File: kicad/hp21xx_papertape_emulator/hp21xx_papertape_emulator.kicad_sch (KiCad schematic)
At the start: 75 parts, among them J1 Micro_SD_Card_Det_Hirose_DM3AT, J2 HP Microcircuit, J3 SWD, J4 SERIAL, Q1 AO3401A, SW1 Up, SW2 Down, SW3 Select, U1 USBLC6-2SC6, U2 TLV75533PDRV, U3 74HCT245, U4 74LVC245, U5 74LVC1G04, U6 STM32F103C8Tx, U7 74AHC1GU04, Y1 8MHz

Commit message: Tried to create production files but it failed...
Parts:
- removed C5: 1u, Capacitor_SMD:C_0805_2012Metric, symbol Device:C_Small
- removed Q1: AO3401A, Package_TO_SOT_SMD:SOT-323_SC-70, symbol Simulation_SPICE:PMOS
- removed R18, R19: 4.7k, Resistor_SMD:R_0402_1005Metric, symbol Device:R_Small
- removed R23: 100k, Resistor_SMD:R_0402_1005Metric, symbol Device:R_Small
- removed R24: 10k, Resistor_SMD:R_0402_1005Metric, symbol Device:R_Small
- added C10, C8, C9: 100n, Capacitor_SMD:C_0402_1005Metric, symbol Device:C_Small
- added C2: 4.7u, Capacitor_SMD:C_1206_3216Metric, symbol Device:C_Small
- added H5, H6, H7, H8: MountingHole, MountingHole:MountingHole_2.2mm_M2, symbol Mechanical:MountingHole
- added R39: 1.8k, Resistor_SMD:R_0603_1608Metric, symbol Device:R_Small
- added R40: 3.3k, Resistor_SMD:R_0402_1005Metric, symbol Device:R_Small
- Brd1: footprint (none) -> Connector_PinHeader_2.54mm:PinHeader_1x04_P2.54mm_Vertical
- H1, H4: footprint MountingHole:MountingHole_2.7mm_M2.5 -> MountingHole:MountingHole_2.2mm_M2
- H2: renamed from H3; footprint MountingHole:MountingHole_2.7mm_M2.5 -> MountingHole:MountingHole_2.2mm_M2
- H3: renamed from H2; footprint MountingHole:MountingHole_2.7mm_M2.5 -> MountingHole:MountingHole_2.2mm_M2
- J3: renamed from J1; footprint (none) -> Connector_Card:microSD_HC_Hirose_DM3AT-SF-PEJM5
- J4: renamed from J2; footprint (none) -> Connector_IDC:IDC-Header_2x10_P2.54mm_Latch_Horizontal
- R11: renamed from R15; LCSC C4109 -> C25104
- R12: renamed from R16; LCSC C4109 -> C3015788
- R13: renamed from R25; LCSC C4109 -> C25104
- R14: renamed from R26; LCSC C4109 -> C3015788
- R15: renamed from R27; LCSC C4109 -> C25104
- R16: renamed from R28; LCSC C4109 -> C3015788
- R17: renamed from R29; LCSC C4109 -> C25104
- R18: renamed from R30; LCSC C4109 -> C3015788
- R24: renamed from R31; LCSC C4109 -> C25104
- R25: renamed from R32; LCSC C4109 -> C3015788
- R27: renamed from R33; LCSC C4109 -> C25104
- R28: renamed from R34; LCSC C4109 -> C3015788
- R33: renamed from R35; LCSC C4109 -> C25104
- R34: renamed from R36; LCSC C4109 -> C3015788
- R35: renamed from R37; LCSC C4109 -> C25104
- R36: renamed from R38; LCSC C4109 -> C3015788
- R37: renamed from R39; LCSC C4109 -> C25104
- R38: renamed from R40; LCSC C4109 -> C3015788
- U3: renamed from U1; LCSC (none) -> C21713975
- U6: renamed from U5; footprint (none) -> Package_TO_SOT_SMD:SOT-23-5; LCSC (none) -> C7827
- Y1: footprint Crystal:Crystal_SMD_HC49-SD -> Crystal:Crystal_SMD_5032-2Pin_5.0x3.2mm; LCSC C20617538 -> C115962
- renumbered C7 to C1, C6 to C3, C10 to C4, C3 to C5, C4 to C6, C12 to C7, D3 to D1, D1 to D3, J3 to J1, J4 to J2, R9 to R1, R41 to R10, R17 to R19, R10 to R2, R3 to R20, R5 to R21, R7 to R22, R11 to R23, R42 to R26, R4 to R29, R13 to R3, R6 to R30, R8 to R31, R12 to R32, R14 to R4, R22 to R5, R20 to R6, R21 to R7, R2 to R8, R1 to R9, SW3 to SW1, SW1 to SW2, SW2 to SW3, U2 to U1, U6 to U2, U7 to U4, U3 to U5, U4 to U7
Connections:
- net +3.3V: now also C8.1, C9.1
- net +5V: now also C10.1, C2.1
- net ENUSB: now also R5.1
- net GND: now also C10.2, C2.2, C8.2, C9.2, R40.1
- net USBACT: now reaches U2.11 (PA1)
- net USBACT: now also R39.1, R40.2
- net at D3.2 (A), U3.5 (VBUS), USB1.11 (VBUS)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: now also R39.2
- no-connect marks 10 -> 9
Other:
- moved on the sheet: D3

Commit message: Almost done. Waiting for confirming OLED display and buttons dimensions.
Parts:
- added C11: 100n, Capacitor_SMD:C_0402_1005Metric, symbol Device:C_Small
- D1, D2, J1, J2, J4, SW1, SW2, SW3: now left out of the parts list
- J3: LCSC (none) -> C114218
- OLED1: renamed from Brd1; now left out of the parts list
- R12, R14, R16, R18, R25, R28, R34, R36, R38: value 820 -> 1k; LCSC C3015788 -> C11702
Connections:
- net +5V: now also C11.1
- net GND: now also C11.2

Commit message: Added paper out handling.
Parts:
- added U8: 74AHCT1G125, Package_TO_SOT_SMD:SOT-23-5, symbol 74xGxx:74LVC1G125
- U4: value 74AHC1GU04 -> 74AHCT1G04SE-7; LCSC C460485 -> C460498
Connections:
- net +5V: now also U8.5 (VCC)
- net GND: now also U8.3 (GND)
- net PUNEN: now also U8.1
- net PAPEROUT: now reaches U2.3 (PC14)
- net PAPEROUT: now also U8.2
- net at J4.11 (Pin_11), U5.13 (B5): now also U8.4
- no-connect marks 9 -> 8

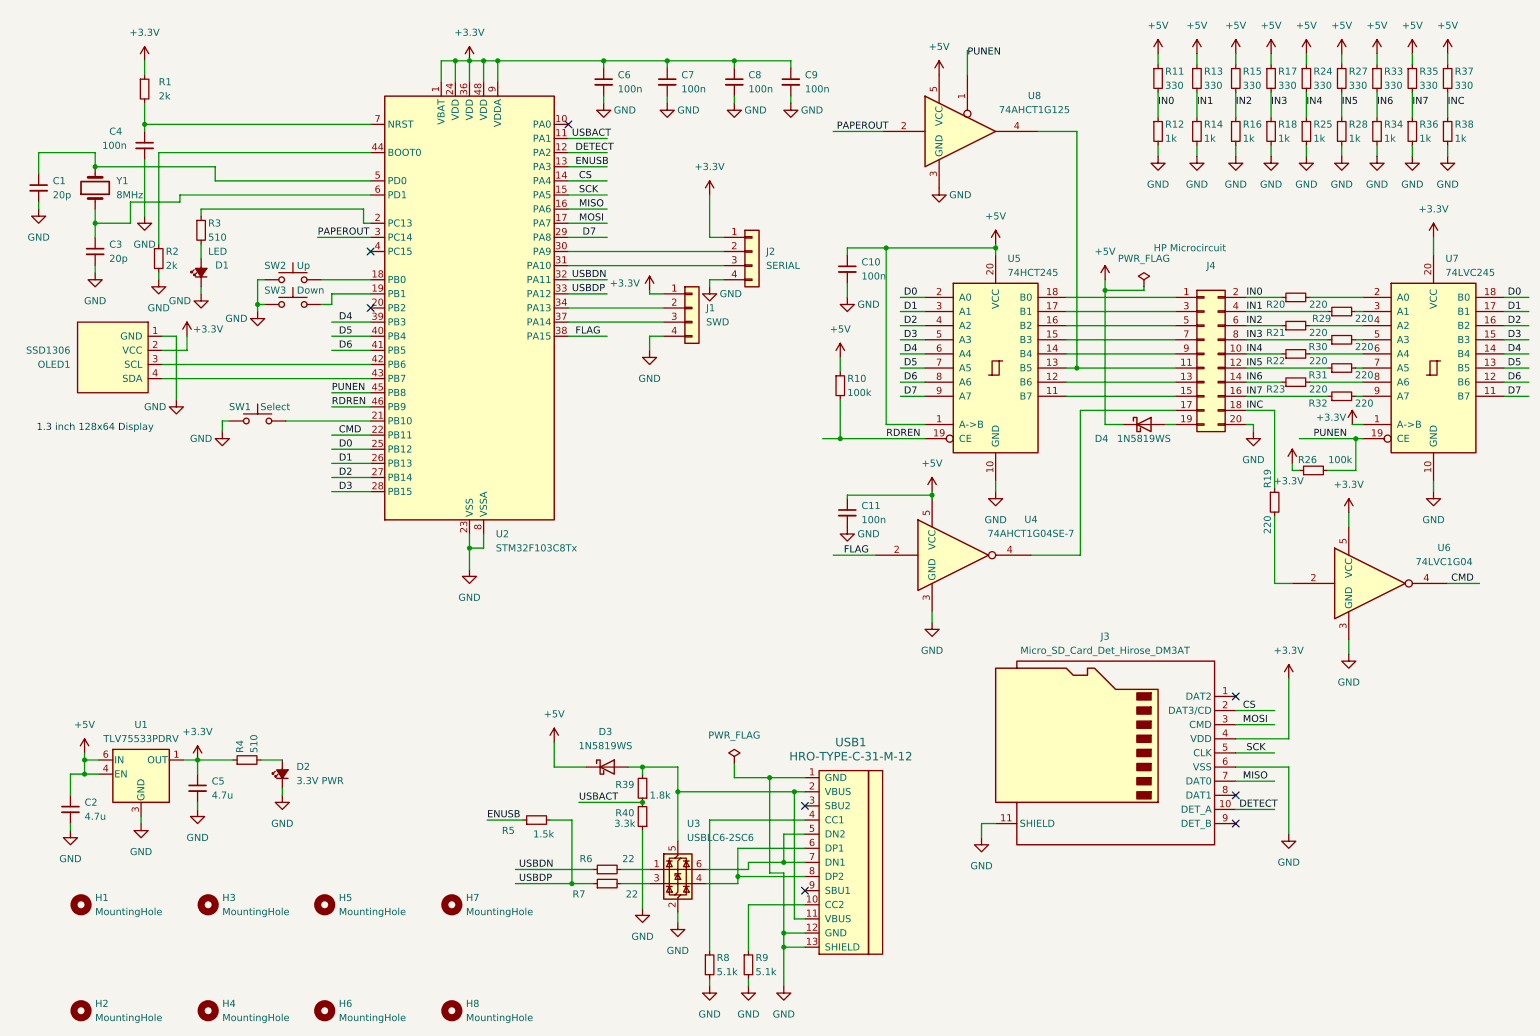
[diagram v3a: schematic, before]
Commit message: Updates to support simultaneous PTR and PTP. Able yo use 540 and 541 instead of 245 if not available.
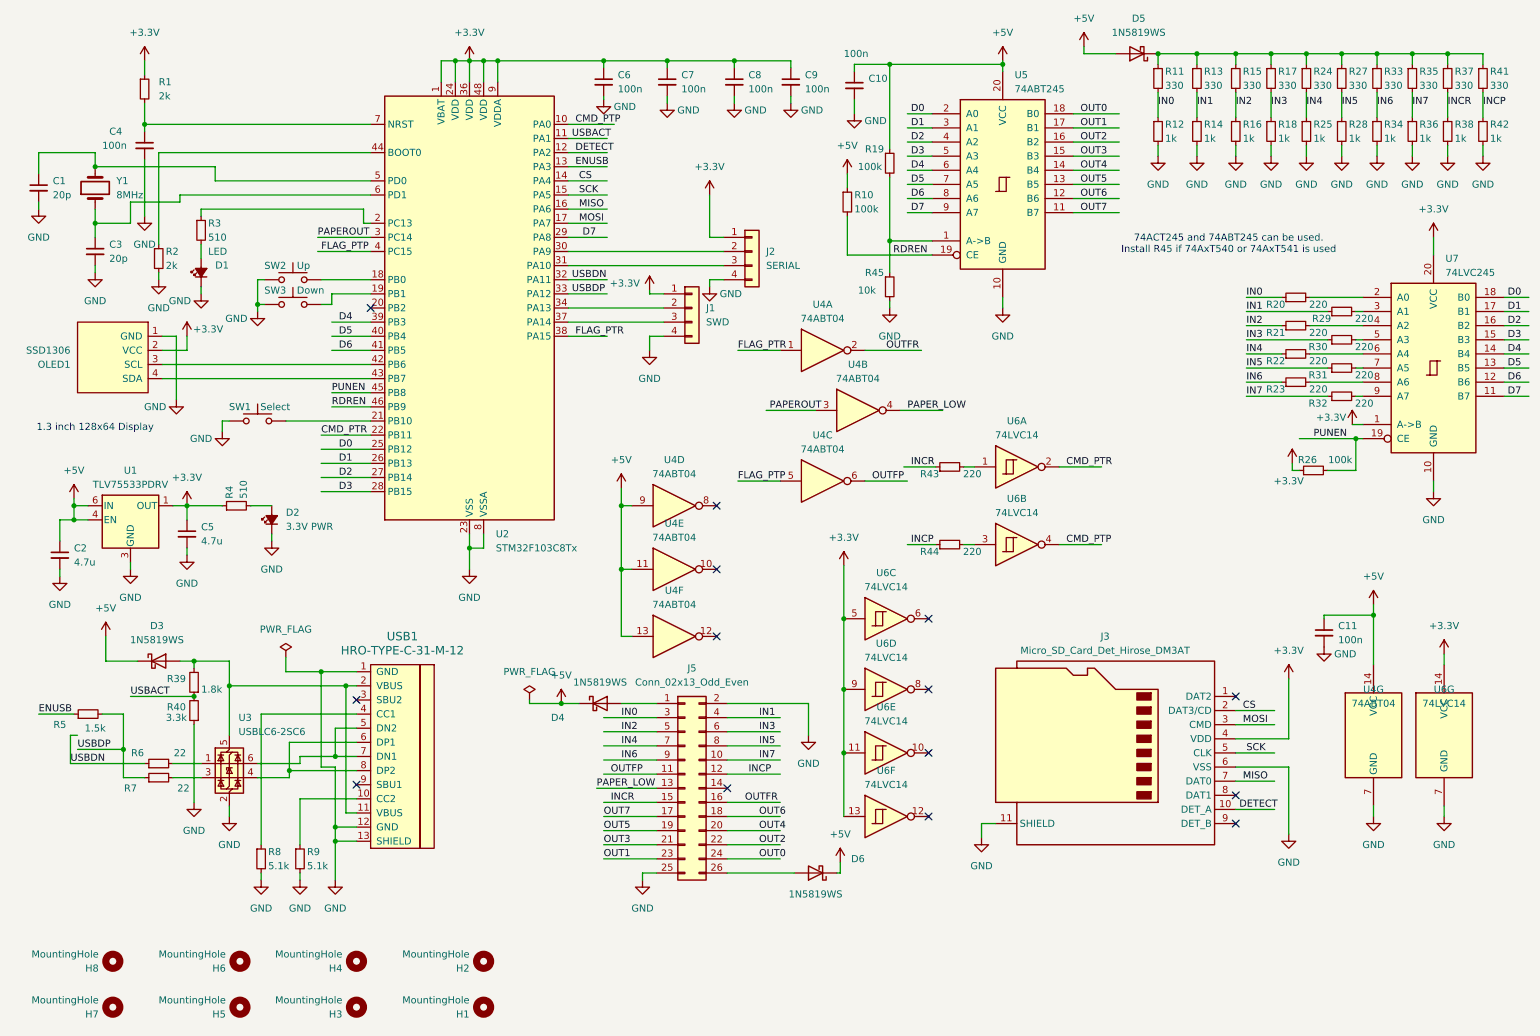
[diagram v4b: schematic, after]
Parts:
- removed J4: HP Microcircuit, Connector_IDC:IDC-Header_2x10_P2.54mm_Latch_Horizontal, symbol Connector_Generic:Conn_02x10_Odd_Even
- removed U4: 74AHCT1G04SE-7, Package_TO_SOT_SMD:SOT-353_SC-70-5, symbol 74xGxx:74LVC1GU04
- removed U6: 74LVC1G04, Package_TO_SOT_SMD:SOT-23-5, symbol 74xGxx:74LVC1G04
- removed U8: 74AHCT1G125, Package_TO_SOT_SMD:SOT-23-5, symbol 74xGxx:74LVC1G125
- added D5, D6: 1N5819WS, Diode_SMD:D_SOD-323, symbol Diode:1N5819WS
- added J5: Conn_02x13_Odd_Even, Connector_IDC:IDC-Header_2x13_P2.54mm_Latch_Horizontal, symbol Connector_Generic:Conn_02x13_Odd_Even
- added R41: 330, Resistor_SMD:R_0402_1005Metric, symbol Device:R_Small
- added R42: 1k, Resistor_SMD:R_0402_1005Metric, symbol Device:R_Small
- added R43, R44: 220, Resistor_SMD:R_0402_1005Metric, symbol Device:R_Small
- added R45: 10k, Resistor_SMD:R_0402_1005Metric, symbol Device:R_Small
- added U4: 74ABT04, Package_SO:TSSOP-14_4.4x5mm_P0.65mm, symbol 74xx:74HCT04
- added U6: 74LVC14, Package_SO:TSSOP-14_4.4x5mm_P0.65mm, symbol 74xx:74HC14
- R19: value 220 -> 100k; LCSC C25091 -> C11702
- U5: value 74HCT245 -> 74ABT245; Comment (none) -> Can also use 74ACT245 LCSC C6931; LCSC C6779 -> C2652111
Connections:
- net +3.3V: now also U6.11, U6.13, U6.14 (VCC), U6.5, U6.9
- net +5V: now also R19.1, D5.2 (A), D6.1 (K), U4.11, U4.13, U4.14 (VCC), U4.9; no longer R11.1, R13.1, R15.1, R17.1, R24.1, R27.1, R33.1, R35.1, R37.1, U5.1 (A->B)
- net GND: now also J5.2 (Pin_2), J5.25 (Pin_25), R42.2, R45.2, U4.7 (GND), U6.7 (GND)
- net IN0: now also J5.3 (Pin_3)
- net IN1: now also J5.4 (Pin_4)
- net IN2: now also J5.5 (Pin_5)
- net IN3: now also J5.6 (Pin_6)
- net IN4: now also J5.7 (Pin_7)
- net IN5: now also J5.8 (Pin_8)
- net IN6: now also J5.9 (Pin_9)
- net IN7: now also J5.10 (Pin_10)
- net PAPEROUT: now also U4.3
- net CMD_PTP: now reaches U2.10 (PA0)
- net CMD_PTP: now also U6.4
- net FLAG_PTP: now reaches U2.4 (PC15)
- net FLAG_PTP: now also U4.5
- net OUT5: now reaches U5.13 (B5)
- net OUT5: now also J5.19 (Pin_19)
- net OUT7: now reaches U5.11 (B7)
- net OUT7: now also J5.17 (Pin_17)
- net OUT6: now reaches U5.12 (B6)
- net OUT6: now also J5.18 (Pin_18)
- net OUT4: now reaches U5.14 (B4)
- net OUT4: now also J5.20 (Pin_20)
- net OUT3: now reaches U5.15 (B3)
- net OUT3: now also J5.21 (Pin_21)
- net OUT2: now reaches U5.16 (B2)
- net OUT2: now also J5.22 (Pin_22)
- net OUT1: now reaches U5.17 (B1)
- net OUT1: now also J5.23 (Pin_23)
- net OUT0: now reaches U5.18 (B0)
- net OUT0: now also J5.24 (Pin_24)
- net at R19.2: now also U5.1 (A->B), R45.1
- net at D4.2 (A): now also J5.1 (Pin_1)
- net CMD renamed CMD_PTR
- net CMD_PTR: now also U6.2
- net FLAG renamed FLAG_PTR
- net FLAG_PTR: now also U4.1
- net INC renamed INCR
- net INCR: now also J5.15 (Pin_15), R43.1; no longer R19.1
- new net: D5.1 (K), R11.1, R13.1, R15.1, R17.1, R24.1, R27.1, R33.1, R35.1, R37.1, R41.1
- new net: R43.2, U6.1
- new net: D6.2 (A), J5.26 (Pin_26)
- new net: R44.2, U6.3
- new net INCP: J5.12 (Pin_12), R41.2, R42.1, R44.1
- new net OUTFP: J5.11 (Pin_11), U4.6
- new net OUTFR: J5.16 (Pin_16), U4.2
- new net PAPER_LOW: J5.13 (Pin_13), U4.4
- no-connect marks 8 -> 14
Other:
- note added: "74ACT245 and 74ABT245 can be used. Install R45 if 74AxT540 or 74AxT541 is used"
- moved on the sheet: C10, C11, C2, C5, D2, D3, D4, H1, H2, H3, H4, H5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

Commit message: Updated to use NMOS drivers instead.
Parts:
- removed U4: 74ABT04, Package_SO:TSSOP-14_4.4x5mm_P0.65mm, symbol 74xx:74HCT04
- removed U5: 74ABT245, Package_SO:TSSOP-20_4.4x6.5mm_P0.65mm, symbol 74xx:74HC245
- added D10, D11, D12, D13, D14, D15, D8, D9: 1N4148, Diode_SMD:D_SOD-323, symbol Device:D_Small
- added D7: 1N5819WS, Diode_SMD:D_SOD-323, symbol Diode:1N5819WS
- added L1: 10uH, Inductor_SMD:L_0805_2012Metric, symbol Device:L_Ferrite_Small
- added Q1, Q10, Q11, Q13, Q14, Q2, Q3, Q4, Q5, Q6, Q7, Q8, Q9: 2N7002, Package_TO_SOT_SMD:SOT-23, symbol Simulation_SPICE:NMOS
- added Q12, Q15: BSS84, symbol Simulation_SPICE:PMOS
- added R100, R101, R102, R103, R94, R95, R96, R97, R98, R99: 1k, Resistor_SMD:R_0402_1005Metric, symbol Device:R_Small
- added R104, R56, R59, R62, R65, R68, R71, R74, R77, R80, R83: 10k, Resistor_SMD:R_0402_1005Metric, symbol Device:R_Small
- added R46, R47, R48, R49, R50, R51, R52, R53: 22, Resistor_SMD:R_0402_1005Metric, symbol Device:R_Small
- added R54, R57, R60, R63, R66, R69, R72, R75, R78, R81, R84, R86, R88, R90: 100, Resistor_SMD:R_0402_1005Metric, symbol Device:R_Small
- added R55, R58, R61, R64, R67, R70, R73, R76, R79, R82, R85, R87, R89, R93: 100k, Resistor_SMD:R_0402_1005Metric, symbol Device:R_Small
- added R91: 86.6k, Resistor_SMD:R_0402_1005Metric, symbol Device:R_Small
- added U4: AP3012, Package_TO_SOT_SMD:SOT-23-5, symbol Regulator_Switching:AP3012
- C10, C11: value 100n -> 1u; footprint Capacitor_SMD:C_0402_1005Metric -> Capacitor_SMD:C_0805_2012Metric; LCSC C1525 -> C28323
- R10: value 100k -> 100; LCSC C25741 -> C25076
- R19: LCSC C11702 -> C25741
- R45: LCSC C11702 -> C25531
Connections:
- net +5V: now also L1.1, Q15.1 (D), R89.1, U4.5 (IN); no longer C11.1, R10.1, R19.1
- net D0: now also R57.1
- net D1: now also R60.1
- net D2: now also R69.1
- net D3: now also R10.1
- net D4: now also R72.1
- net D5: now also R75.1
- net D6: now also R78.1
- net D7: now also R81.1
- net FLAG_PTP: now also R54.1
- net FLAG_PTR: now also R63.1
- net GND: now also R19.2, Q1.3 (S), Q10.3 (S), Q11.3 (S), Q13.3 (S), Q14.3 (S), Q2.3 (S), Q3.3 (S), Q4.3 (S), Q5.3 (S), Q6.3 (S), Q7.3 (S), Q8.3 (S), Q9.3 (S), R104.2, R55.2, R58.2, R61.2, R64.2, R67.2, R70.2, R73.2, R76.2, R79.2, R82.2, R87.2, R93.2, U4.2 (GND); no longer R45.2
- net OUT0: now also Q2.1 (D), R49.2, R59.2, R94.2; no longer J5.24 (Pin_24)
- net OUT1: now also Q3.1 (D), R53.1, R62.2; no longer J5.23 (Pin_23)
- net OUT2: now also Q6.1 (D), R101.2, R48.2, R71.2; no longer J5.22 (Pin_22)
- net OUT3: now also R45.2, Q7.1 (D), R102.2, R52.1; no longer J5.21 (Pin_21)
- net OUT4: now also Q8.1 (D), R103.2, R47.2, R74.2; no longer J5.20 (Pin_20)
- net OUT5: now also Q9.1 (D), R100.2, R51.1, R77.2; no longer J5.19 (Pin_19)
- net OUT6: now also Q10.1 (D), R46.2, R80.2, R99.2; no longer J5.18 (Pin_18)
- net OUT7: now also Q11.1 (D), R50.1, R83.2, R98.2; no longer J5.17 (Pin_17)
- net OUTFP: now also Q1.1 (D), R56.2, R95.2
- net OUTFR: now also Q4.1 (D), R65.2, R96.2
- net PAPEROUT: now also R66.1
- net PAPER_LOW: now also Q5.1 (D), R68.2, R97.2
- net RDREN: now also D10.1 (K), D11.1 (K), D12.1 (K), D13.1 (K), D14.1 (K), D15.1 (K), D8.1 (K), D9.1 (K); no longer R10.2
- net PU12V: now reaches R45.1
- net PU12V: now also Q15.3 (S), R56.1, R59.1, R62.1, R65.1, R68.1, R71.1, R74.1, R77.1, R80.1, R83.1; no longer R19.2
- net PUSEL: now reaches U2.20 (PB2)
- net PUSEL: now also R86.1, U4.4 (~{SHDN})
- new net: D15.2 (A), Q8.2 (G), R72.2, R73.1
- new net: J5.18 (Pin_18), R46.1
- new net: D13.2 (A), Q6.2 (G), R69.2, R70.1
- new net: D14.2 (A), Q7.2 (G), R10.2, R19.1
- new net: D11.2 (A), Q10.2 (G), R78.2, R79.1
- new net: Q13.2 (G), R86.2, R87.1
- new net: J5.24 (Pin_24), R49.1
- new net: Q4.2 (G), R63.2, R64.1
- new net: Q14.2 (G), R88.2, R93.1
- new net: D12.2 (A), Q9.2 (G), R75.2, R76.1
- new net: Q5.2 (G), R66.2, R67.1
- new net: D10.2 (A), Q11.2 (G), R81.2, R82.1
- new net: D9.2 (A), Q3.2 (G), R60.2, R61.1
- new net: J5.19 (Pin_19), R51.2
- new net: R104.1, R91.2, U4.3 (FB)
- new net: D8.2 (A), Q2.2 (G), R57.2, R58.1
- new net: Q15.2 (G), R90.2
- new net: Q12.2 (G), R84.2
- new net: Q14.1 (D), R89.2, R90.1
- new net: Q1.2 (G), R54.2, R55.1
- new net: D7.2 (A), L1.2, U4.1 (SW)
- new net: J5.20 (Pin_20), R47.1
- new net: Q13.1 (D), R84.1, R85.2, R88.1
- new net: J5.23 (Pin_23), R53.2
- new net: J5.17 (Pin_17), R50.2
- new net: J5.21 (Pin_21), R52.2
- new net: J5.22 (Pin_22), R48.1
- new net +12V: C11.1, D7.1 (K), Q12.1 (D), R85.1, R91.1
- new net PU5V: Q12.3 (S), R100.1, R101.1, R102.1, R103.1, R94.1, R95.1, R96.1, R97.1, R98.1, R99.1
- no-connect marks 14 -> 10
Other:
- note removed: "74ACT245 and 74ABT245 can be used. Install R45 if 74AxT540 or 74AxT541 is used"
- moved on the sheet: D4, D6, J3, J5, R43, R44, SW2, SW3, U6A, U6B, U6C, U6D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

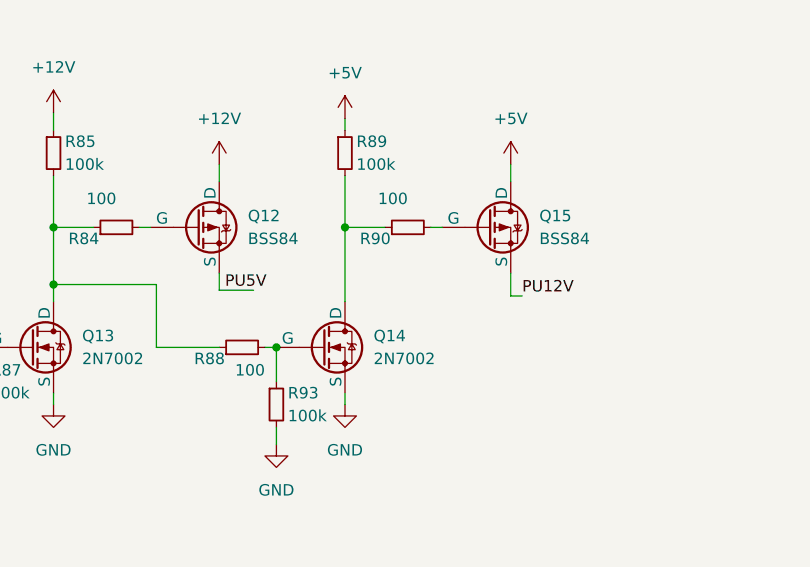
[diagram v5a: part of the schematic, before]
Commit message: Updated to use NMOS drivers instead.
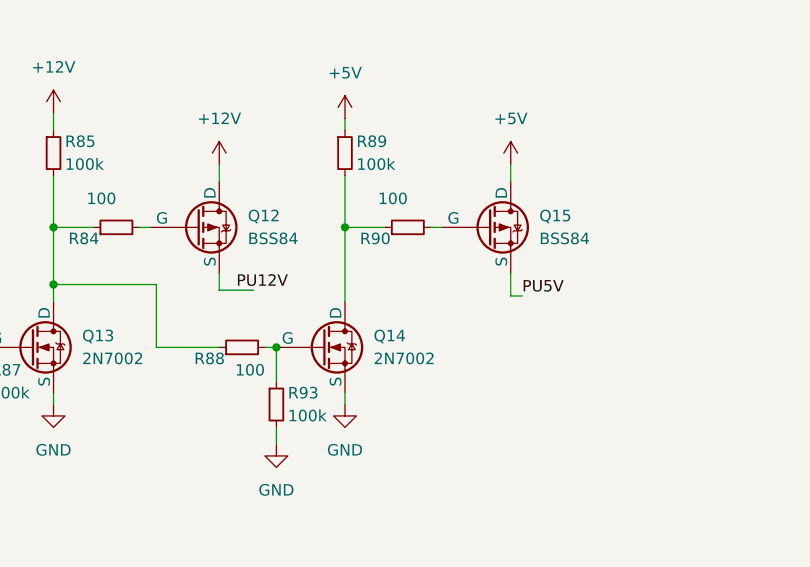
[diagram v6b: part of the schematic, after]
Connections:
- net PU12V: now also Q12.3 (S); no longer Q15.3 (S)
- net PU5V: now also Q15.3 (S); no longer Q12.3 (S)
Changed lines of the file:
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@@
 	)
 	(label "PU12V"
-		(at 300.355 180.975 0)
+		(at 268.605 180.34 0)
 		(effects
 			(font
@@
 	)
 	(label "PU5V"
-		(at 267.335 180.34 0)
-		(effects
-			(font
+		(at 300.355 180.975 0)
+		(effects
+			(font
